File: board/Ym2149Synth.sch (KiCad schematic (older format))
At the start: 14 parts, among them IC1 6n138, J1 AUDIO OUT, P1 MIDI IN, U1 Teensy_3.1, U2 YM2149F, U3 ECS-100

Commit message: Teensy 3.1 -> 3.2
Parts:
- U1: value Teensy_3.1 -> Teensy_3.2
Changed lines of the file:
@@
 P 4400 4350
 F 0 "U1" H 5050 3200 60  0000 C CNN
-F 1 "Teensy_3.1" H 4400 5000 60  0000 C CNN
+F 1 "Teensy_3.2" H 4400 5000 60  0000 C CNN
 F 2 "" H 4500 3750 60  0000 C CNN
 F 3 "" H 4500 3750 60  0000 C CNN

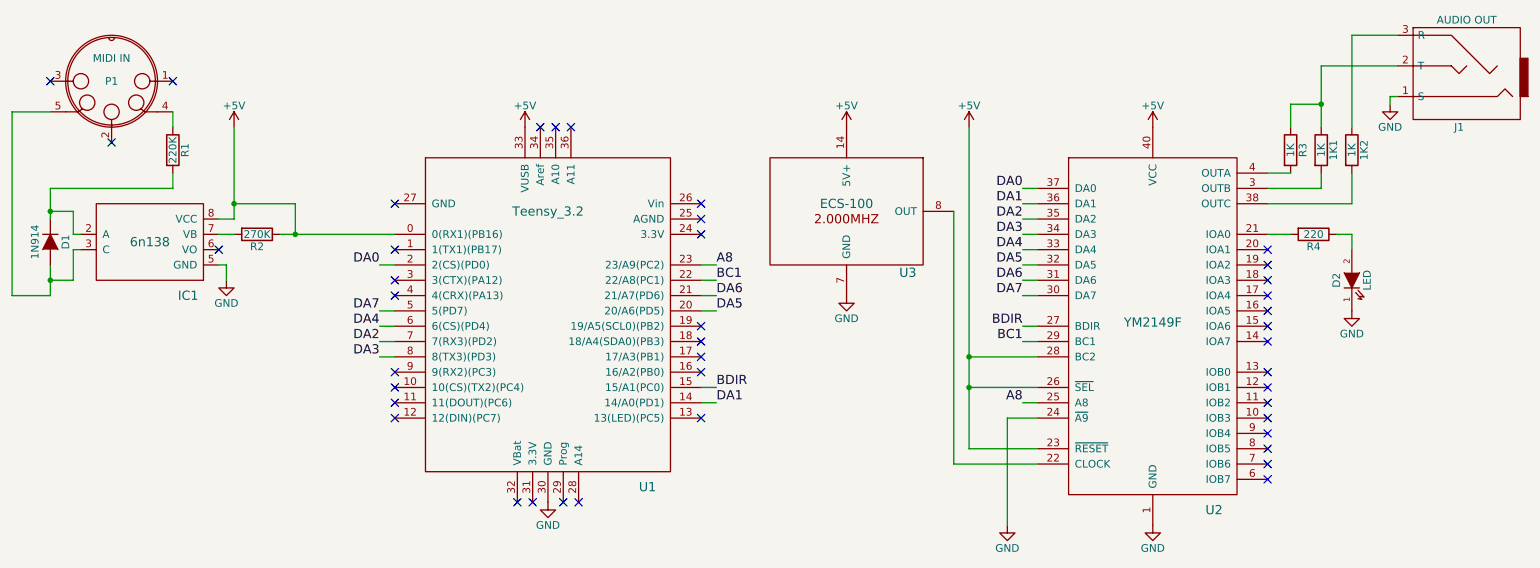
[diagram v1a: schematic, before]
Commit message: Error on schematic. R2 misplaced.
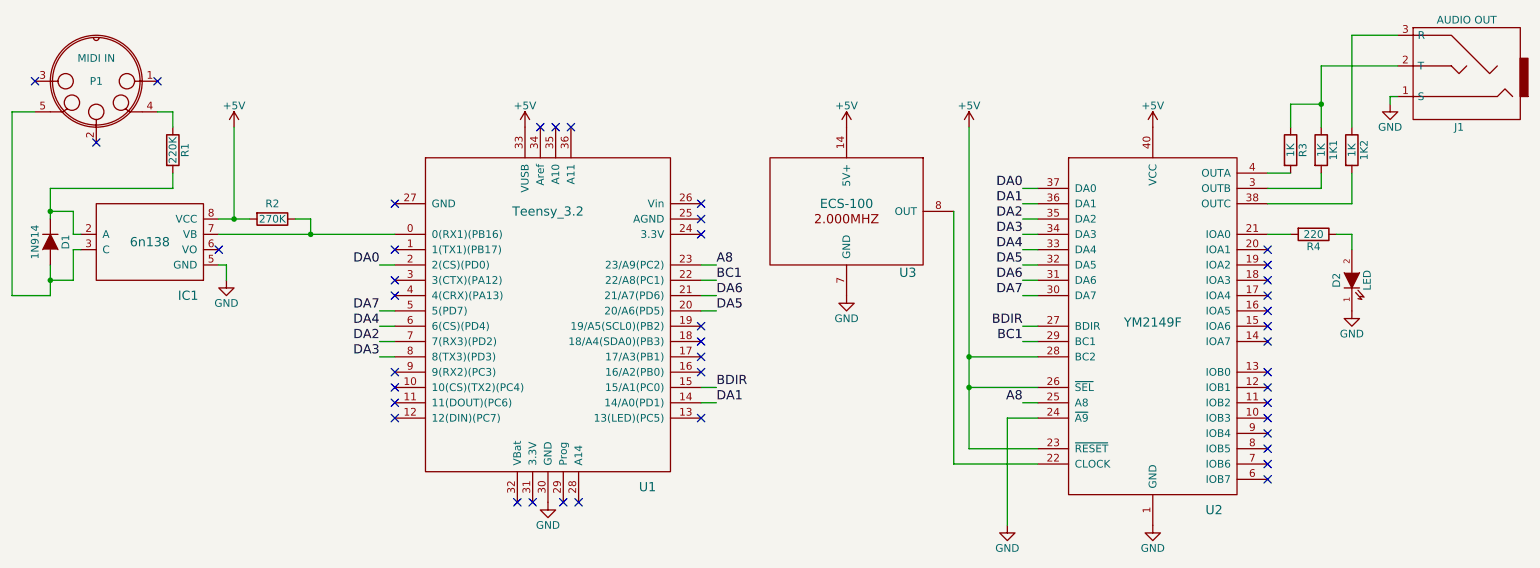
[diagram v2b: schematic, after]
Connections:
- net +5V: now also R2.2; no longer R2.1, U1.0 (0(RX1)(PB16))
- net at IC1.7 (VB): now also R2.1, U1.0 (0(RX1)(PB16)); no longer R2.2
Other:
- moved on the sheet: P1, R2
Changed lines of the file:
@@
 L DIN_5 P1
 U 1 1 57C4BC72
-P 1550 2850
-F 0 "P1" H 1550 2850 50  0000 C CNN
-F 1 "MIDI IN" H 1550 2700 50  0000 C CNN
-F 2 "" H 1550 2850 50  0000 C CNN
-F 3 "" H 1550 2850 50  0000 C CNN
-	1    1550 2850
+P 1450 2850
+F 0 "P1" H 1450 2850 50  0000 C CNN
+F 1 "MIDI IN" H 1450 2700 50  0000 C CNN
+F 2 "" H 1450 2850 50  0000 C CNN
+F 3 "" H 1450 2850 50  0000 C CNN
+	1    1450 2850
 	-1   0    0    1
 $EndComp
@@
 L R R2
 U 1 1 57C4D0D7
-P 2500 3850
-F 0 "R2" V 2580 3850 50  0000 C CNN
-F 1 "270K" V 2500 3850 50  0000 C CNN
-F 2 "" V 2430 3850 50  0000 C CNN
-F 3 "" H 2500 3850 50  0000 C CNN
-	1    2500 3850
+P 2600 3750
+F 0 "R2" V 2500 3750 50  0000 C CNN
+F 1 "270K" V 2600 3750 50  0000 C CNN
+F 2 "" V 2530 3750 50  0000 C CNN
+F 3 "" H 2600 3750 50  0000 C CNN
+	1    2600 3750
 	0    1    1    0
 $EndComp
@@
 NoConn ~ 4550 3150
 NoConn ~ 2250 3950
-NoConn ~ 1150 2850
-NoConn ~ 1550 3250
-NoConn ~ 1950 2850
+NoConn ~ 1050 2850
+NoConn ~ 1450 3250
+NoConn ~ 1850 2850
 NoConn ~ 9100 5450
 NoConn ~ 9100 5350
@@
 	7150 5250 7600 5250
 Wire Wire Line
-	7150 3150 7150 5250
+	7150 3150 7150 4650
+Wire Wire Line
+	7150 4650 7150 4850
+Wire Wire Line
+	7150 4850 7150 5250
 Wire Wire Line
 	7600 4650 7150 4650
@@
 	9100 3450 9250 3450
 Wire Wire Line
-	9450 2750 9450 3150
+	9450 2750 9450 3000
+Wire Wire Line
+	9450 3000 9450 3150
 Wire Wire Line
 	9450 2750 9950 2750
@@
 	1950 3050 1950 3150
 Wire Wire Line
-	1150 3550 1150 3750
+	1150 3550 1150 3700
+Wire Wire Line
+	1150 3700 1150 3750
 Wire Wire Line
 	1150 3550 1950 3550
@@
 Connection ~ 1150 3700
 Wire Wire Line
-	1150 3050 900  3050
+	1050 3050 900  3050
 Wire Wire Line
 	900  3050 900  4250
 Wire Wire Line
-	900  4250 1150 4250
-Wire Wire Line
-	1150 4250 1150 4050
+	1150 4250 900  4250
+Wire Wire Line
+	1150 4050 1150 4150
+Wire Wire Line
+	1150 4150 1150 4250
 Wire Wire Line
 	1300 4150 1150 4150
 Connection ~ 1150 4150
 Wire Wire Line
-	2250 3850 2350 3850
-Wire Wire Line
-	2650 3850 3400 3850
-Wire Wire Line
-	2750 3650 2750 3850
-Connection ~ 2750 3850
-Wire Wire Line
-	2350 3750 2250 3750
-Wire Wire Line
-	2350 3150 2350 3750
-Wire Wire Line
-	2750 3650 2350 3650
-Connection ~ 2350 3650
+	2250 3850 2850 3850
+Wire Wire Line
+	2850 3850 3400 3850
+Wire Wire Line
+	2250 3750 2350 3750
+Wire Wire Line
+	2350 3750 2450 3750
 Wire Wire Line
 	9100 3850 9250 3850
@@
 	1    0    0    -1
 $EndComp
+Connection ~ 2850 3850
+Wire Wire Line
+	2850 3750 2850 3850
+Wire Wire Line
+	2750 3750 2850 3750
+Connection ~ 2350 3750
+Wire Wire Line
+	2350 3750 2350 3150
+Wire Wire Line
+	1950 3050 1850 3050
 $EndSCHEMATC

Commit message: Error in schematic, 6n138 was on wrong output pin.
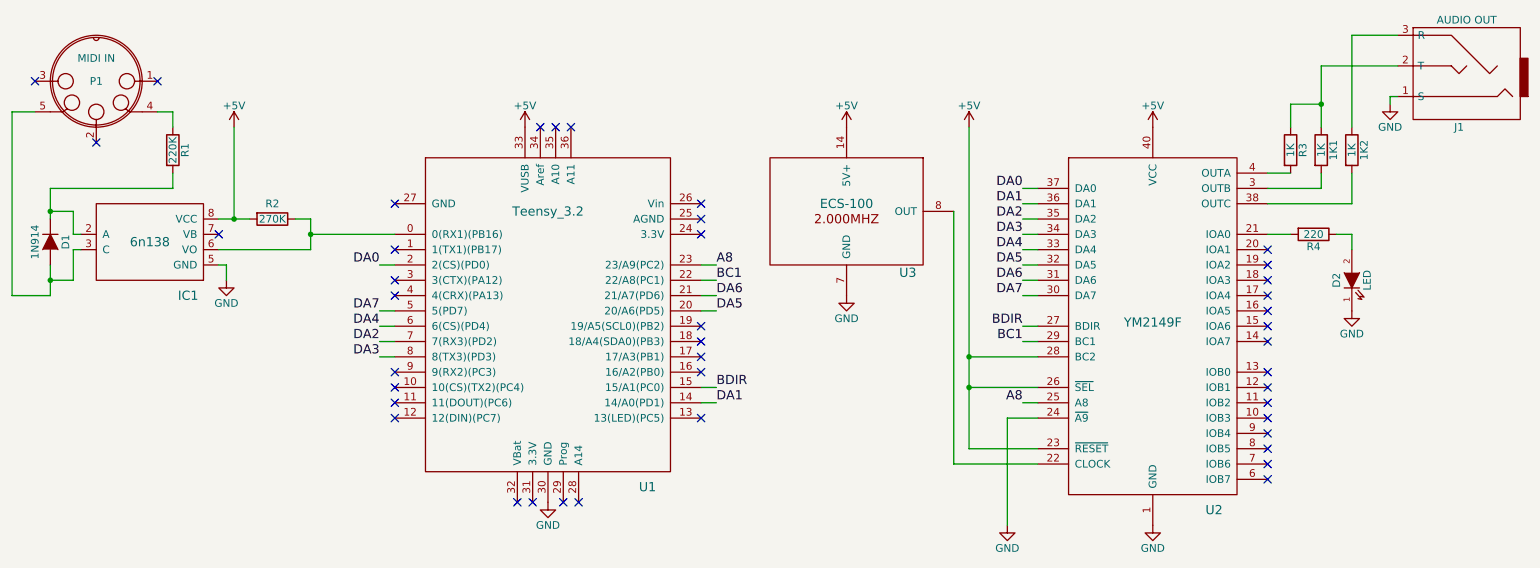
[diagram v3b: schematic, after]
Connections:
- net at R2.1, U1.0 (0(RX1)(PB16)): now also IC1.6 (VO); no longer IC1.7 (VB)
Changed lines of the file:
@@
 NoConn ~ 4450 3150
 NoConn ~ 4550 3150
-NoConn ~ 2250 3950
+NoConn ~ 2250 3850
 NoConn ~ 1050 2850
 NoConn ~ 1450 3250
@@
 	7150 5250 7600 5250
 Wire Wire Line
-	7150 3150 7150 4650
-Wire Wire Line
-	7150 4650 7150 4850
-Wire Wire Line
-	7150 4850 7150 5250
+	7150 3150 7150 5250
 Wire Wire Line
 	7600 4650 7150 4650
@@
 	9100 3450 9250 3450
 Wire Wire Line
-	9450 2750 9450 3000
-Wire Wire Line
-	9450 3000 9450 3150
+	9450 2750 9450 3150
 Wire Wire Line
 	9450 2750 9950 2750
@@
 	1950 3050 1950 3150
 Wire Wire Line
-	1150 3550 1150 3700
-Wire Wire Line
-	1150 3700 1150 3750
+	1150 3550 1150 3750
 Wire Wire Line
 	1150 3550 1950 3550
@@
 	1150 4250 900  4250
 Wire Wire Line
-	1150 4050 1150 4150
-Wire Wire Line
-	1150 4150 1150 4250
+	1150 4050 1150 4250
 Wire Wire Line
 	1300 4150 1150 4150
 Connection ~ 1150 4150
 Wire Wire Line
-	2250 3850 2850 3850
-Wire Wire Line
 	2850 3850 3400 3850
 Wire Wire Line
-	2250 3750 2350 3750
-Wire Wire Line
-	2350 3750 2450 3750
+	2250 3750 2450 3750
 Wire Wire Line
 	9100 3850 9250 3850
@@
 Connection ~ 2850 3850
 Wire Wire Line
-	2850 3750 2850 3850
+	2850 3750 2850 3950
 Wire Wire Line
 	2750 3750 2850 3750
@@
 Wire Wire Line
 	1950 3050 1850 3050
+Wire Wire Line
+	2850 3950 2250 3950
 $EndSCHEMATC
